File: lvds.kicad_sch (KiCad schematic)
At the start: 97 parts, among them J15 Conn_FFC_Amphenol_62684-40210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

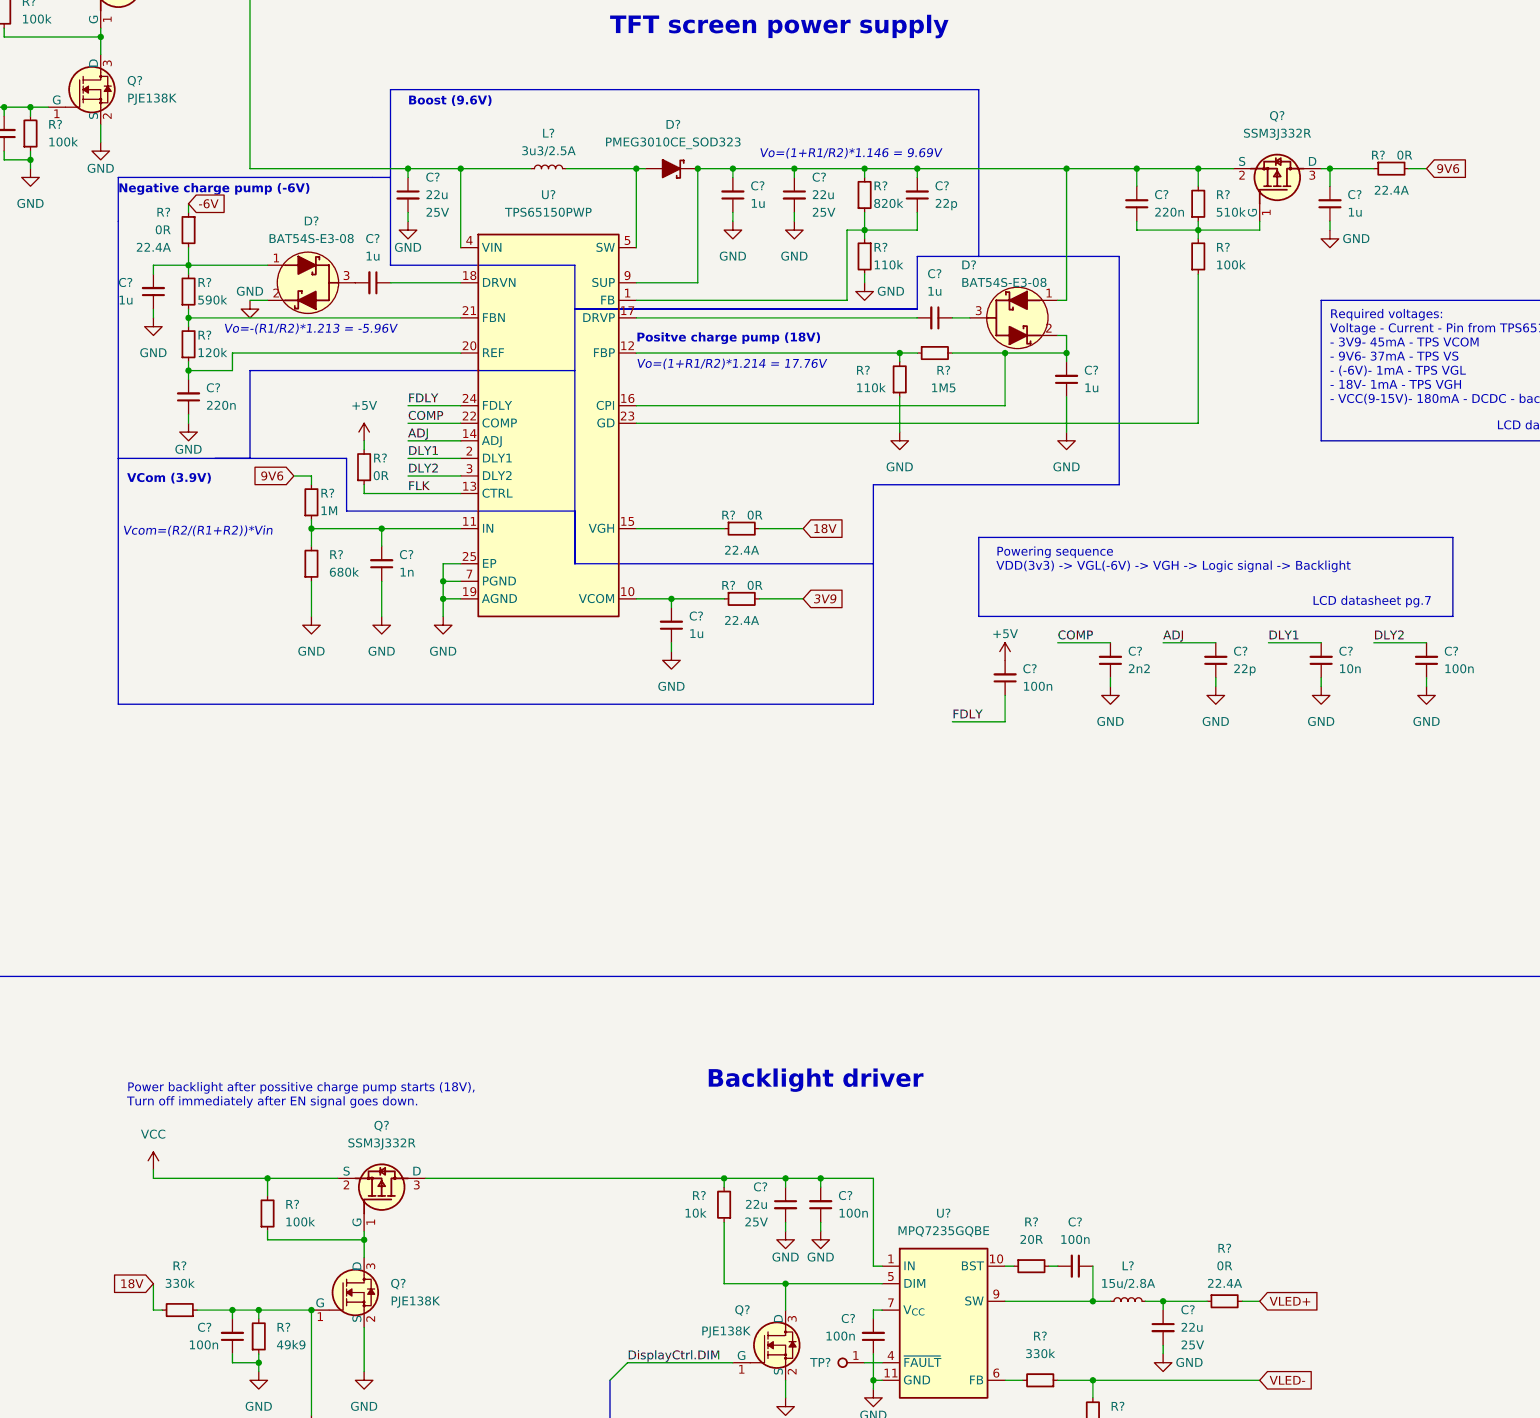
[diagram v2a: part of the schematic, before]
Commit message: [#54617] Reduce resistors diversity (switch size to 0402)
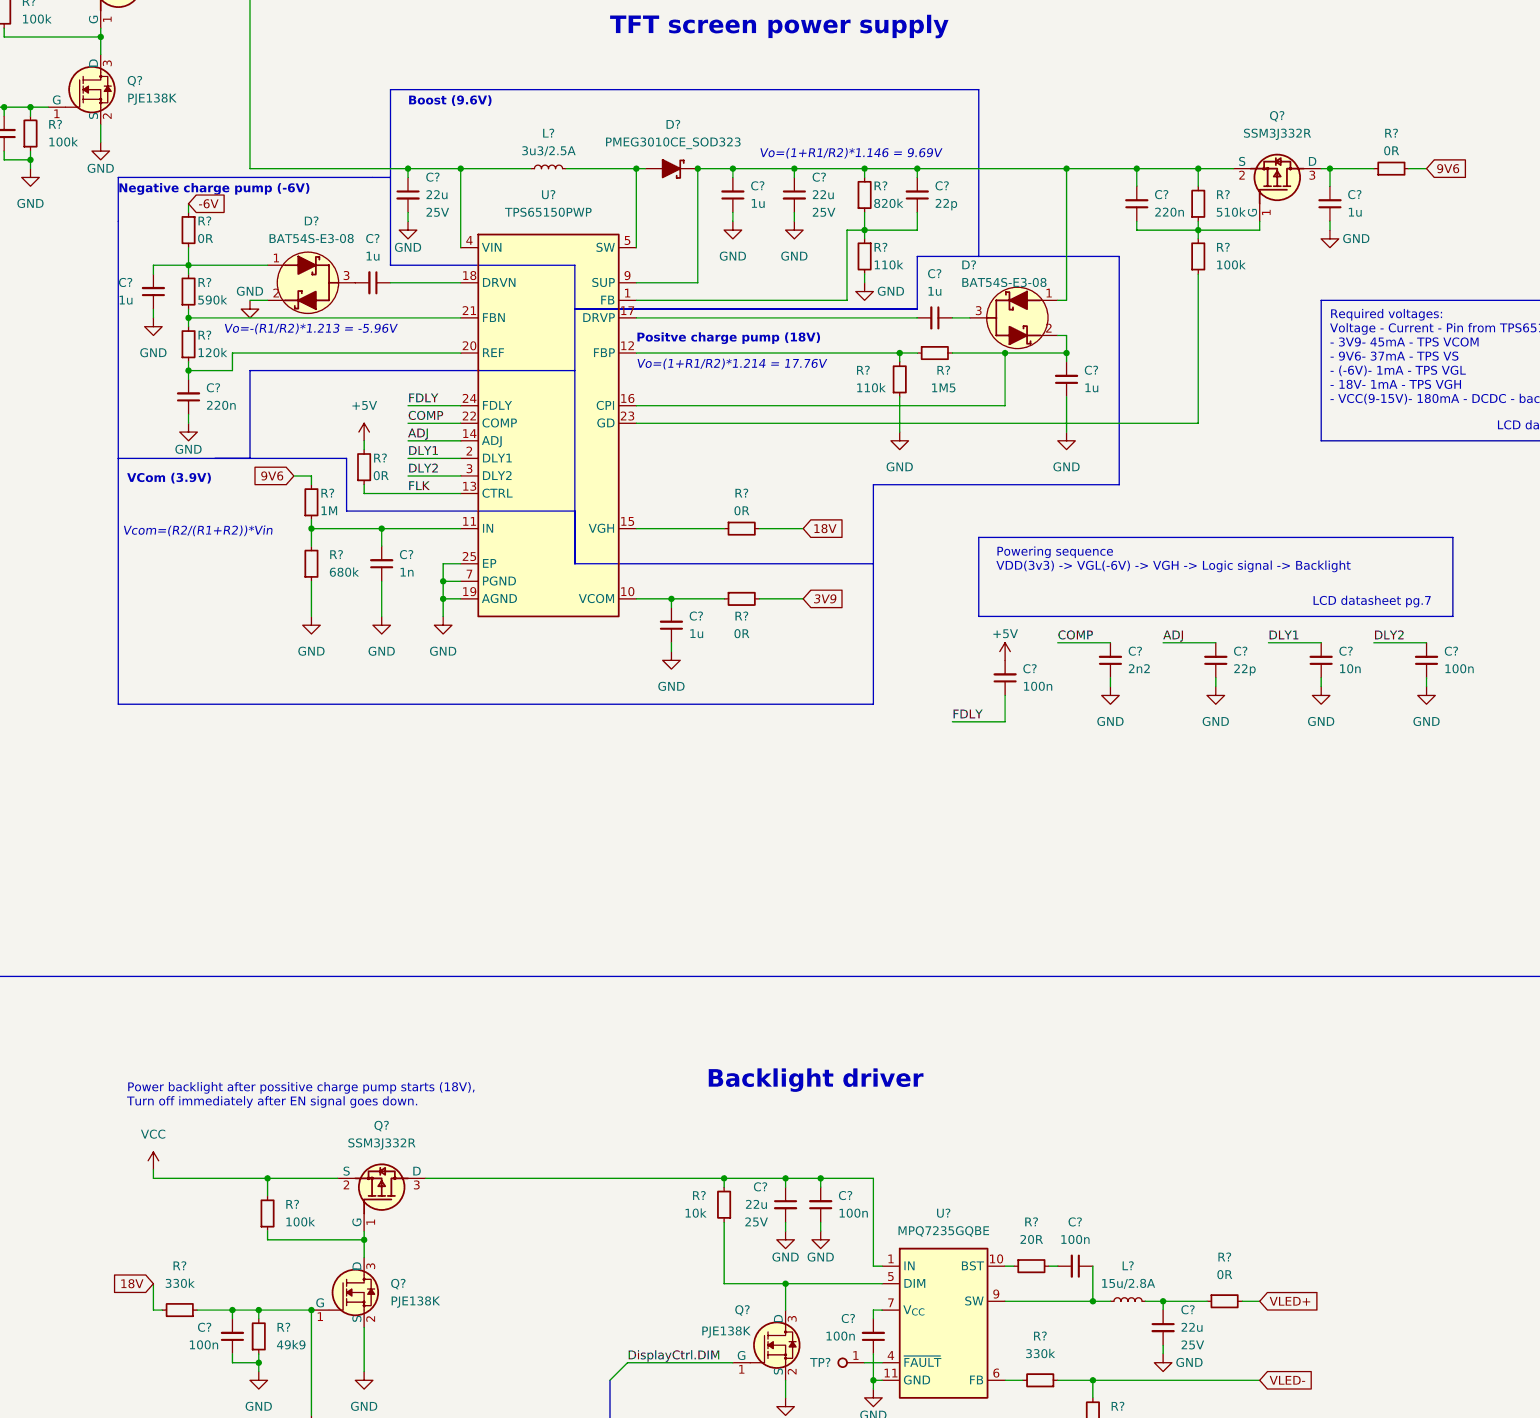
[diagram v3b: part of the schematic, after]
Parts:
- removed R? (x5): R_0R_22.4A_0603, antmicro-footprints:R_0603_1608Metric, symbol antmicroResistors0603:R_0R_22.4A_0603
- removed R?: R_1R2_0603, antmicro-footprints:R_0603_1608Metric, symbol antmicroResistors0603:R_1R2_0603
- added R? (x5): R_0R_0402, antmicro-footprints:R_0402_1005Metric, symbol antmicroResistors0402:R_0R_0402
- added R?: R_1R2_0402, antmicro-footprints:R_0402_1005Metric, symbol antmicroResistors0402:R_1R2_0402
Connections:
- net -6V: now also R?.1
- net 18V: now also R?.2
- net 3V9: now also R?.2
- net 9V6: now also R?.2
- net GND: now also R?.1
- net VLED+: now also R?.2
- net VLED-: now also R?.2
- net at C?.2, Q?.3 (D): now also R?.1
- net at C?.1, L?.2: now also R?.1
- net at C?.2, D?.1, R?.2: now also R?.2
- net at U?.15 (VGH): now also R?.1
- net at C?.2, U?.10 (VCOM): now also R?.1

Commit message: [#54617] NFC: mark matching network as DNP & add note about it
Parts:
- L?: DNP (none) -> DNP
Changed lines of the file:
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@@
       (effects (font (size 1.27 1.27) (thickness 0.15)) (justify left bottom) hide)
+    )
+    (property "DNP" "DNP" (id 12) (at 137.16 49.53 0)
+      (effects (font (size 1.27 1.27)) hide)
     )
     (pin "1")

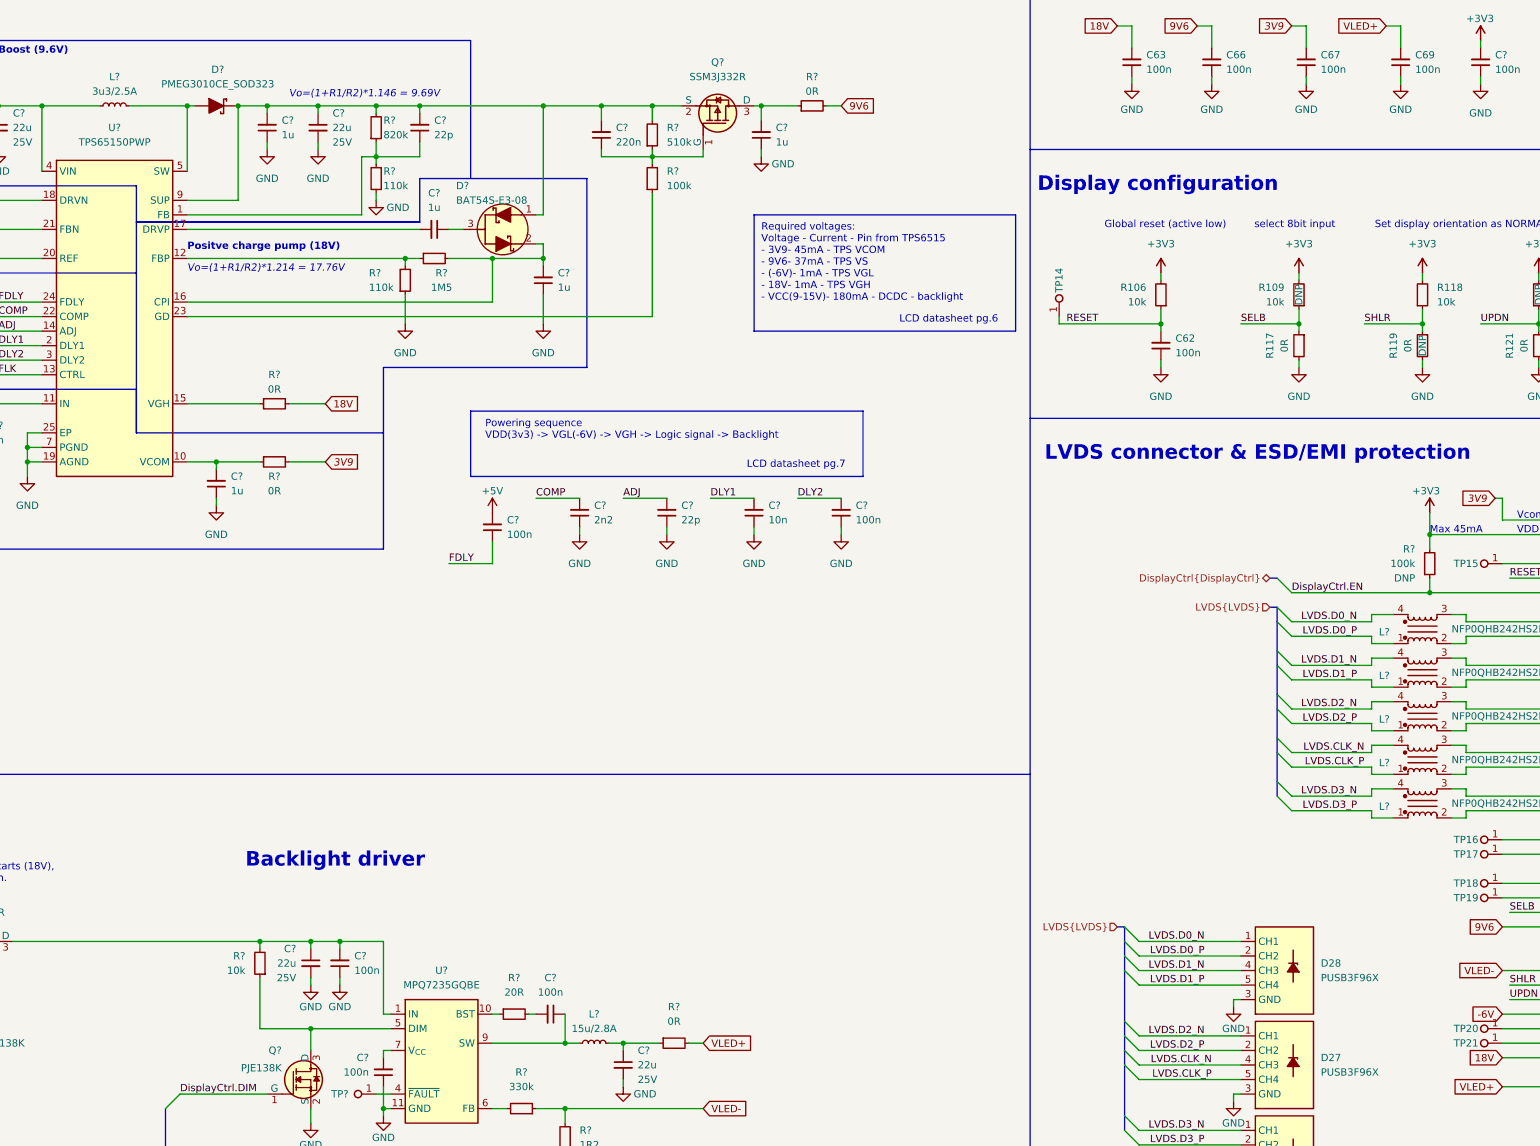
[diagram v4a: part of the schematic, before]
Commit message: [#54617] Migrate to KiCad 7
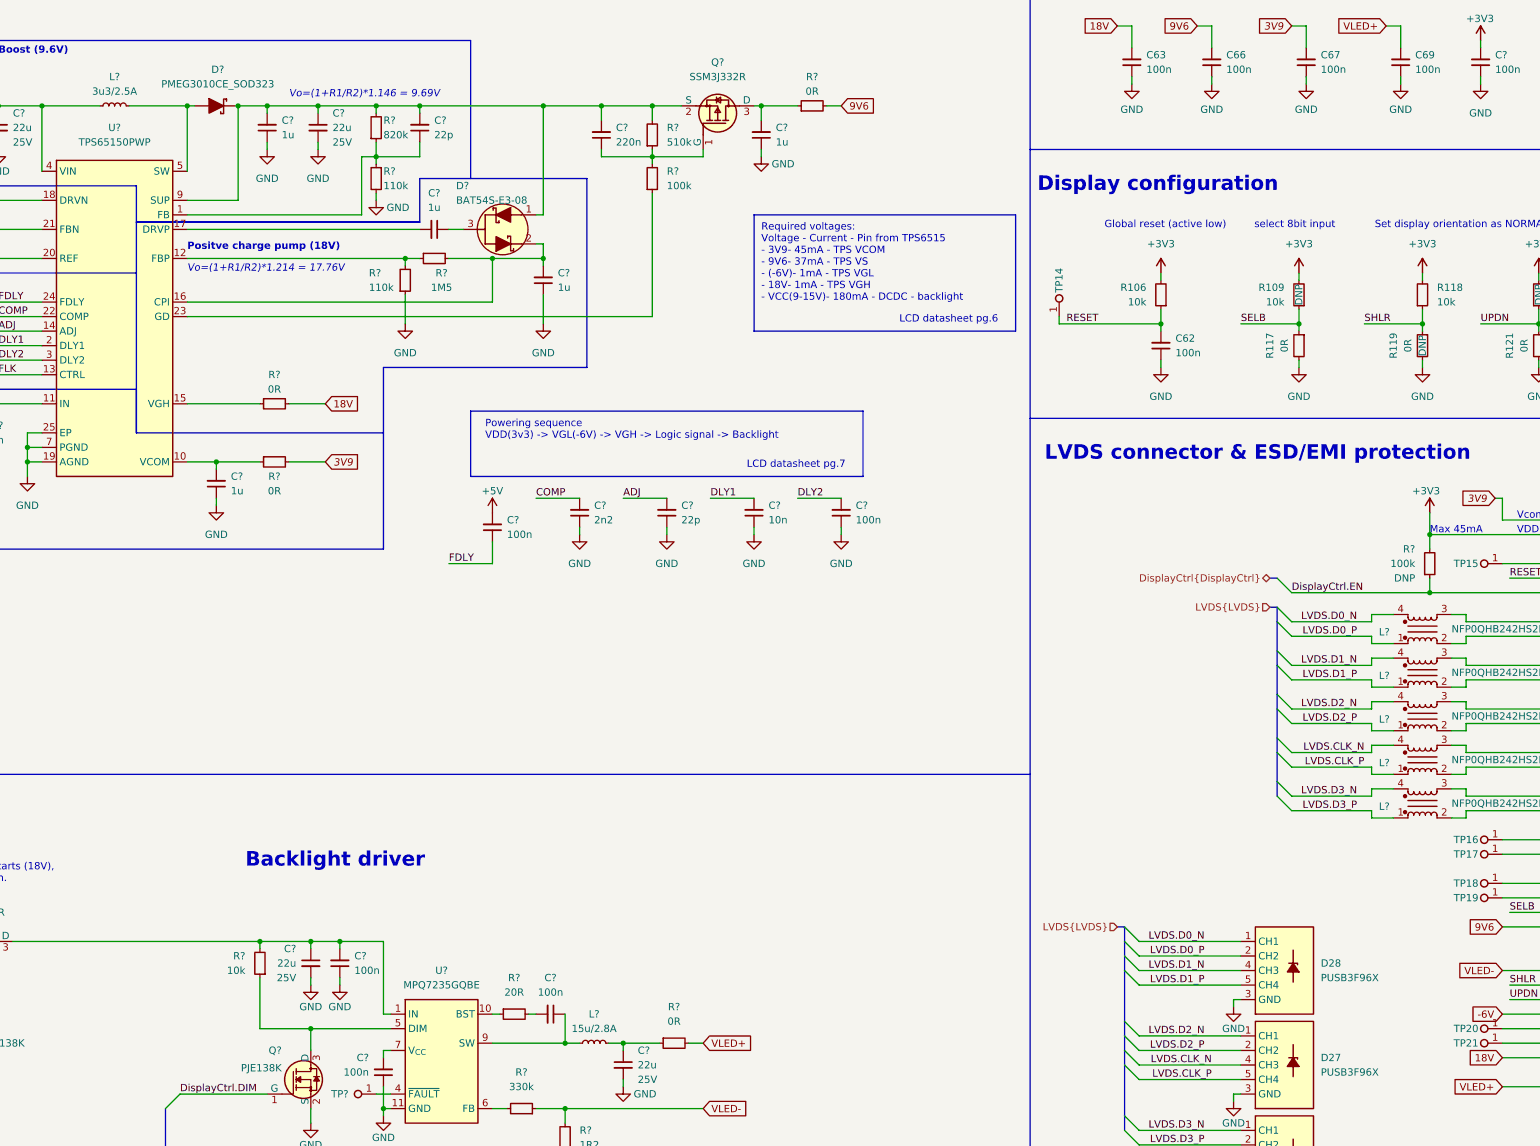
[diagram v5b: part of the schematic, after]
